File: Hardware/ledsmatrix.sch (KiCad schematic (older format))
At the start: 69 parts

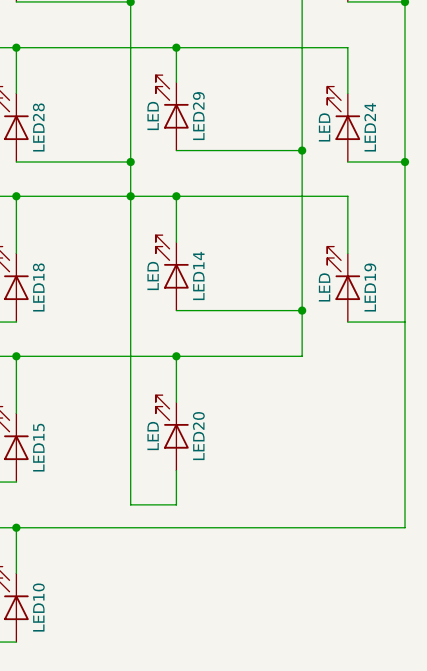
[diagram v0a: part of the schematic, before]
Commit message: Bugfix for swm_col9
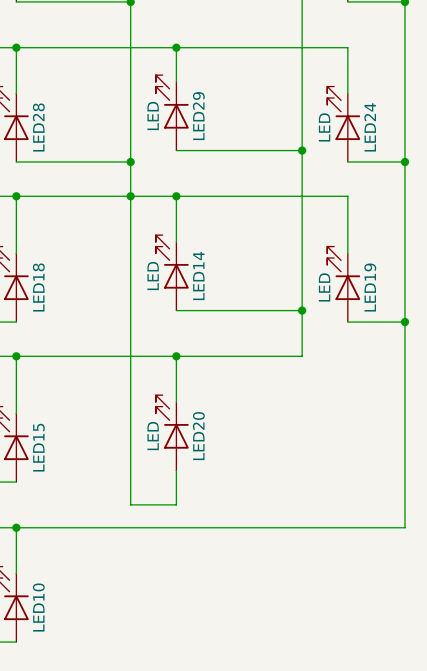
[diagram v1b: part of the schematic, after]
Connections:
- net CA9: now also LED19.2 (A)
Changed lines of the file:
@@
 Connection ~ 6250 2700
-Wire Wire Line
-	6450 5550 6700 5550
 Wire Wire Line
 	6450 4150 6700 4150
@@
 	5500 3450 5500 4150
 Wire Wire Line
-	6700 4850 6700 6450
+	6700 4850 6700 5550
+Wire Wire Line
+	6450 5550 6700 5550
+Connection ~ 6700 5550
+Wire Wire Line
+	6700 5550 6700 6450
 $EndSCHEMATC

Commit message: add driling holes
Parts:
- LED1, LED10, LED11, LED12, LED13, LED14, LED15, LED16, LED17, LED18, LED19, LED2, LED20, LED21, LED22, LED23, LED24, LED25, LED26, LED27, LED28, LED29, LED3, LED30, LED31, LED32, LED33, LED34, LED35, LED36, LED37, LED38, LED39, LED4, LED40, LED41, LED42, LED43, LED44, LED45, LED46, LED47, LED48, LED49, LED5, LED50, LED51, LED52, LED53, LED54, LED55, LED56, LED57, LED58, LED59, LED6, LED60, LED61, LED62, LED63, LED64, LED65, LED66, LED67, LED68, LED69, LED7, LED8, LED9: symbol Device:LED -> Mechanical-Keyboard-rescue:LED-Device
